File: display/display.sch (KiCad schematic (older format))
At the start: 18 parts, among them IC1 CD40109BE, IC2 CD40109BE, IC3 CD40109BE, IC4 CD40109BE, U1 LP2950-3.0_TO92, U2 74LS244

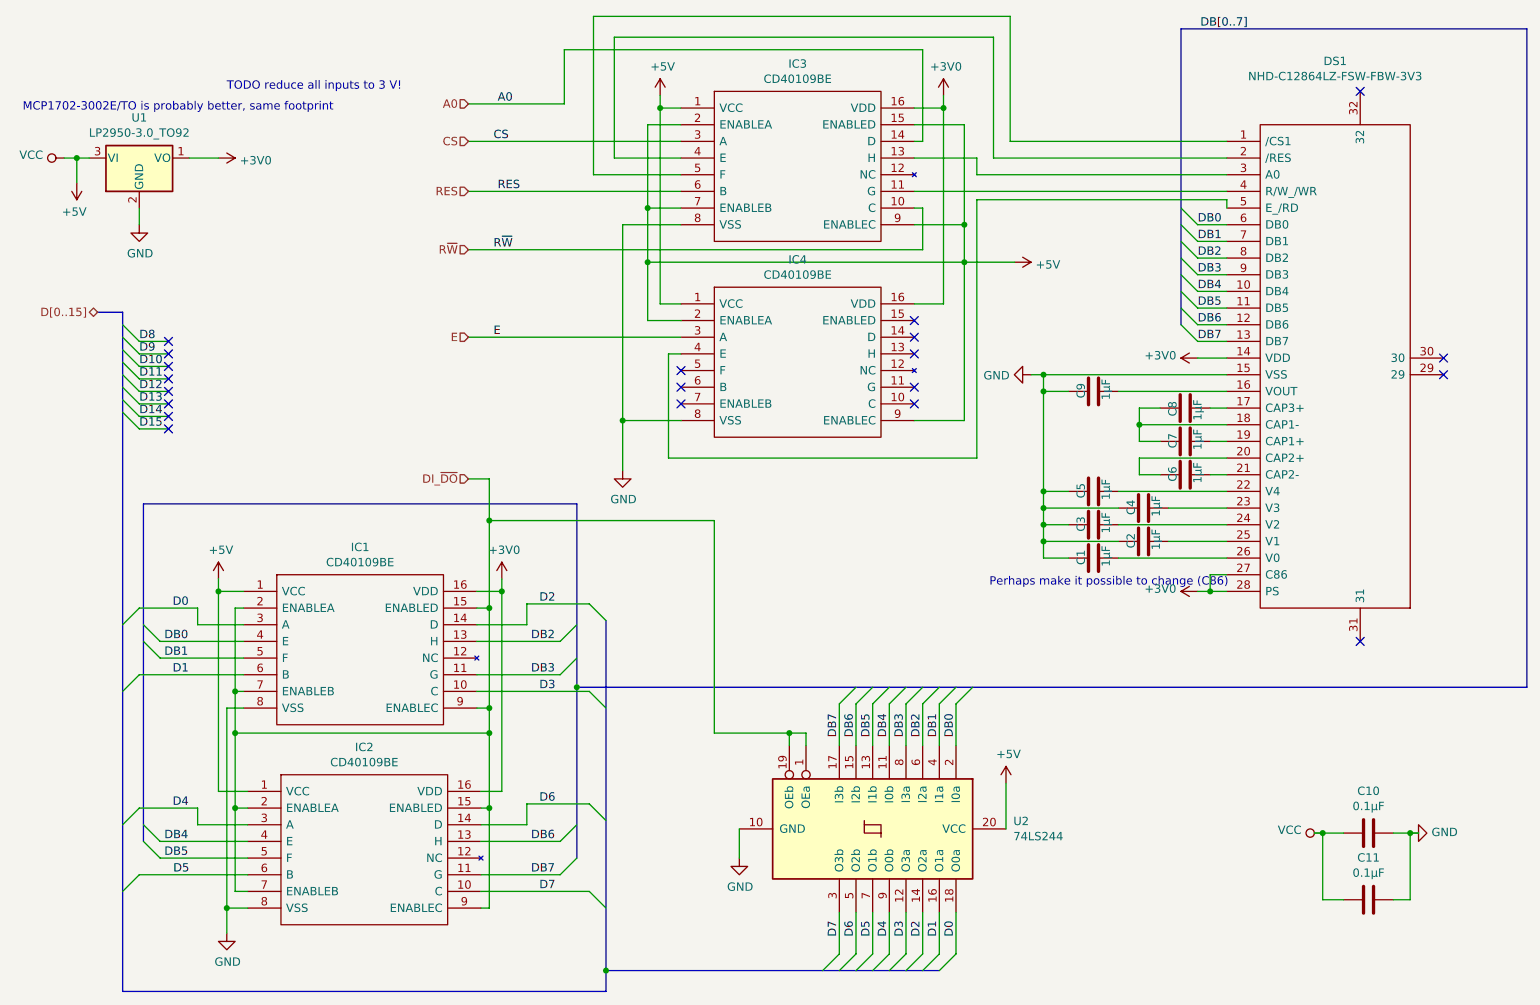
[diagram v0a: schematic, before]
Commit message: add bit operations
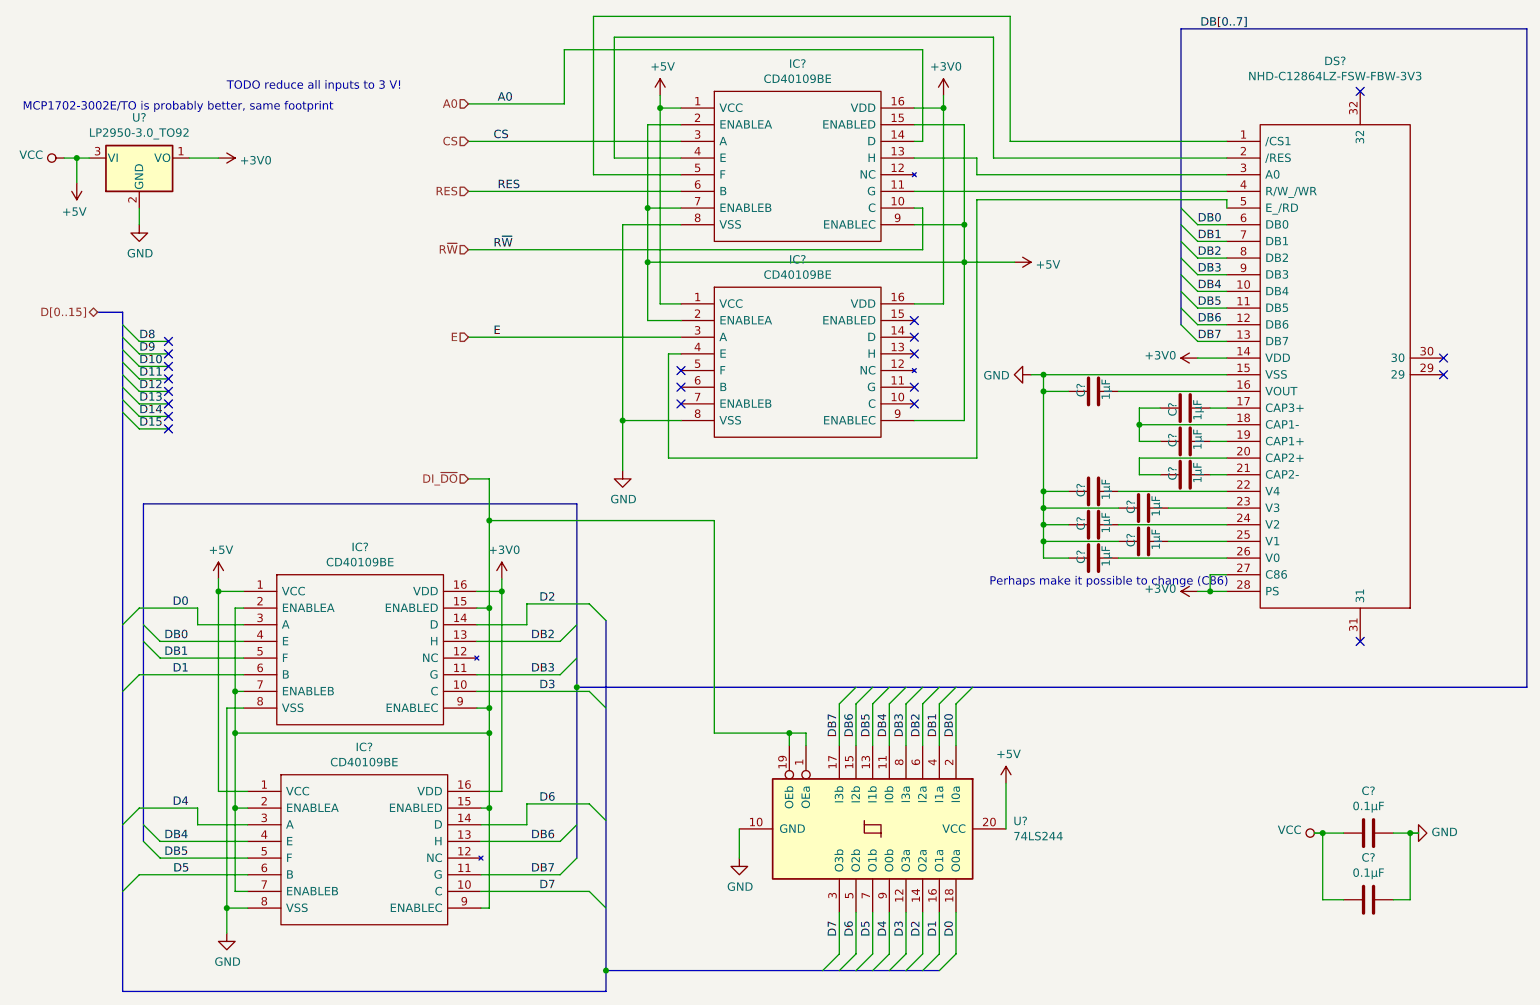
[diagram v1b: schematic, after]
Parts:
- renumbered C8 to C?, C7 to C?, C9 to C?, C6 to C?, C5 to C?, C4 to C?, C3 to C?, C2 to C?, C1 to C?, C10 to C?, C11 to C?, DS1 to DS?, IC3 to IC?, IC4 to IC?, IC1 to IC?, IC2 to IC?, U2 to U?, U1 to U?

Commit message: part lists
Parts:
- gave numbers to parts that had none: 18
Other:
- note added: "TODO CONNECT TO GROUND"
